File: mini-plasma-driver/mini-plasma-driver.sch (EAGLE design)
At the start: 36 parts, among them IC1 IR21844D, IC2 74LS19N, IC3 NE555N, Q1 IRF640, Q2 IRF640, Q3 2N2369, Q4 2N2369

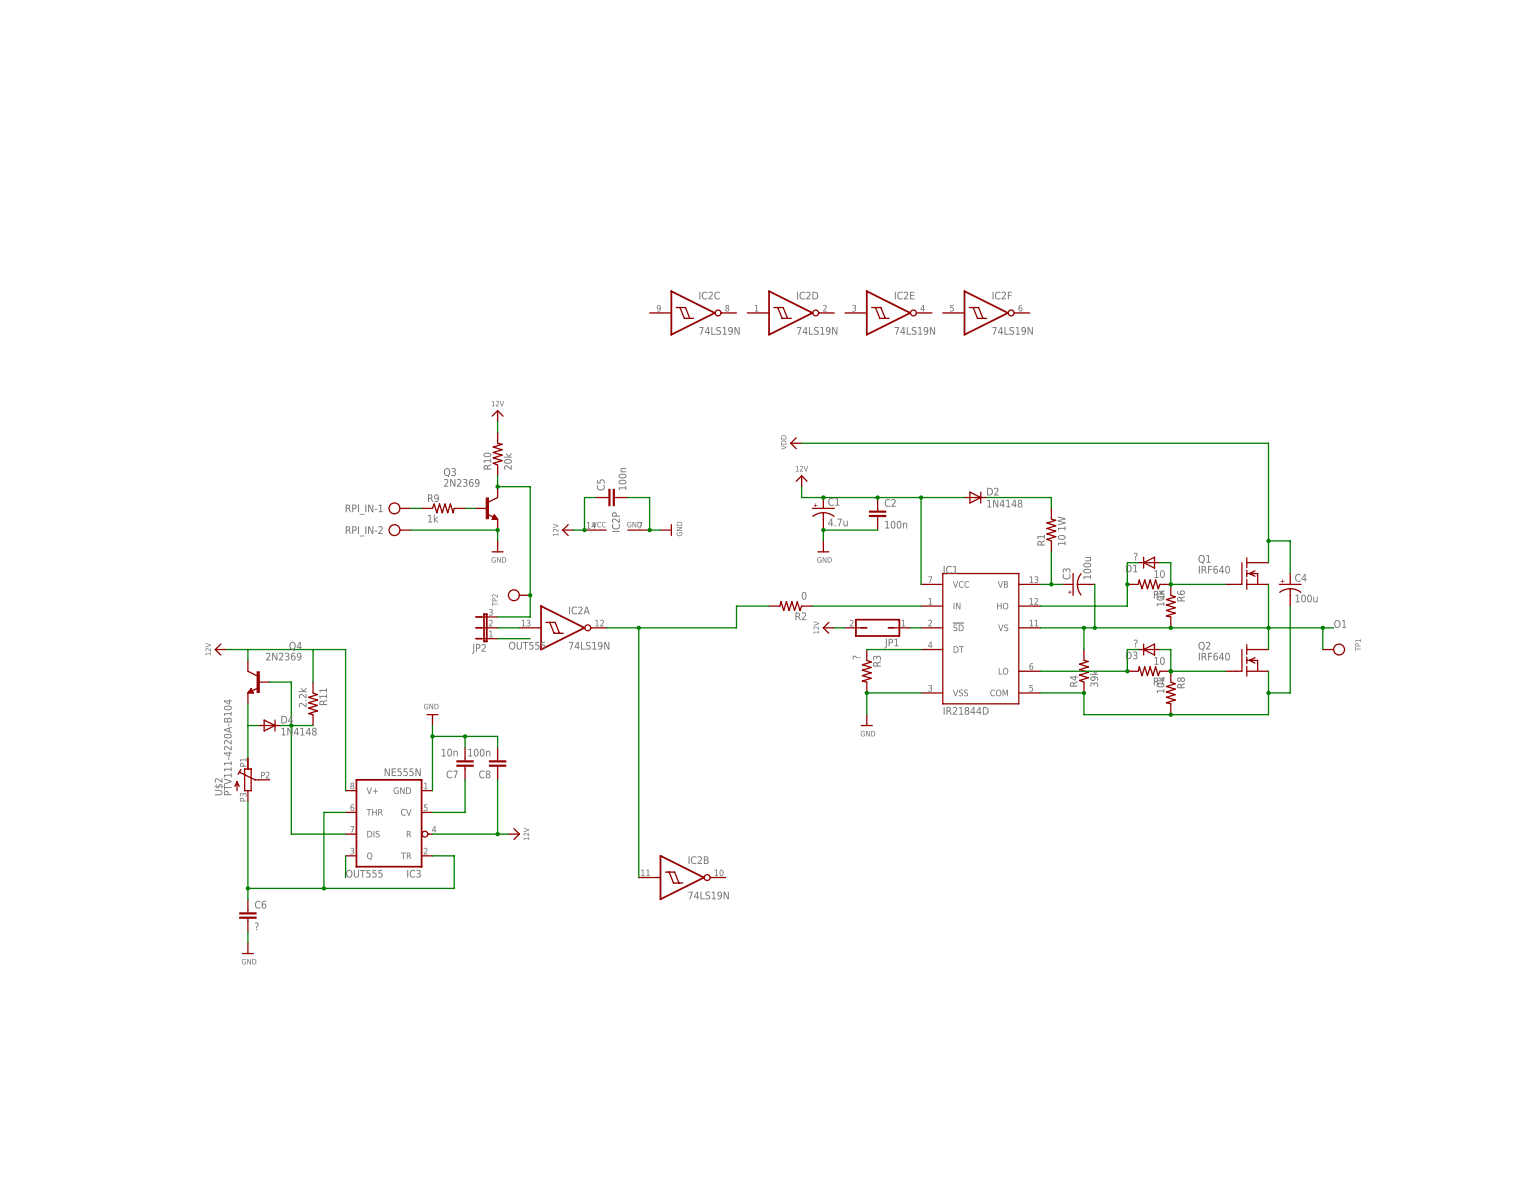
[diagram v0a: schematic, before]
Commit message: mini-plasma-driver
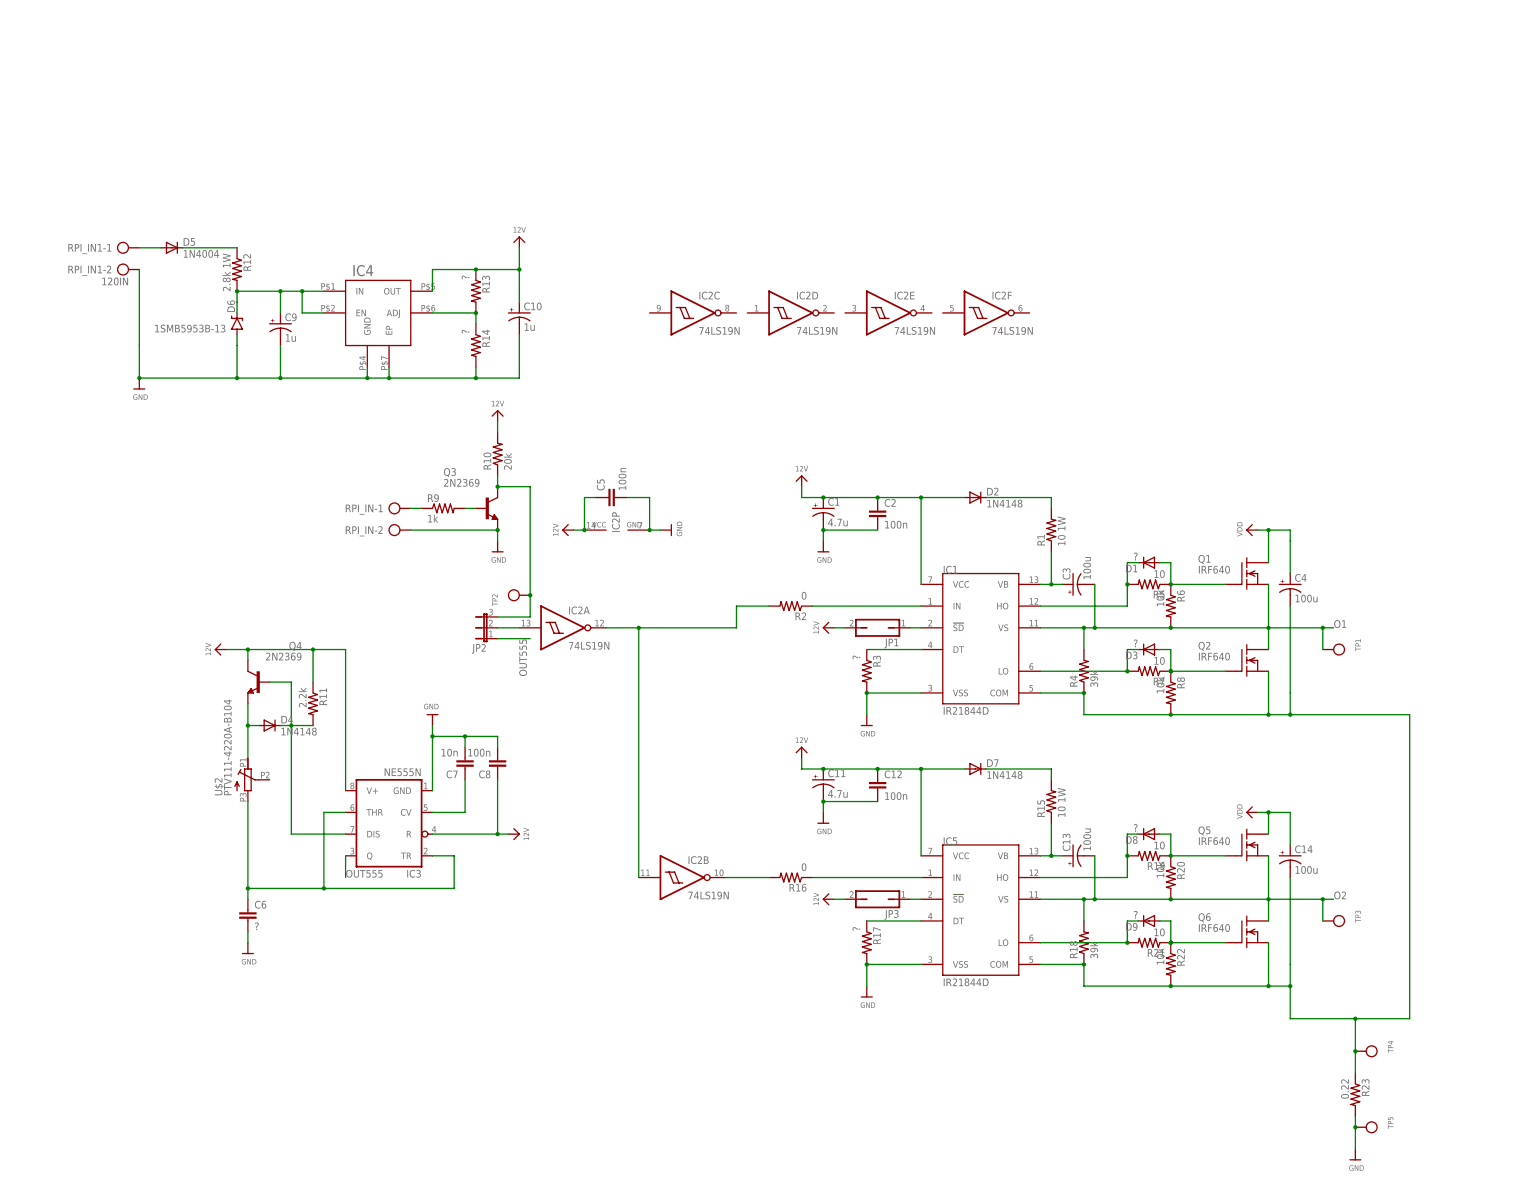
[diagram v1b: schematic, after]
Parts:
- added C10, C9: 1u, rcl:CPOL-USE2.5-5
- added C11: 4.7u, rcl:CPOL-USE2.5-5
- added C12: 100n, rcl:C-EU025-025X050
- added C13, C14: 100u, rcl:CPOL-USE3.5-10
- added D5: 1N4004, adafruit:1N4004
- added D6: 1SMB5953B-13, SparkFun-DiscreteSemi:DIODE-ZENERSMB
- added D7: 1N4148, diode:1N4148DO35-10
- added D8, D9: ?, diode:1N4148DO35-10
- added IC4: NCP781IC, keves-ng:NCP781IC
- added IC5: IR21844D, irs:IR21844D
- added JP3: (no value), jumper:JP1Q
- added Q5, Q6: IRF640, transistor-fet:IRF620
- added R12: 2.8k 1W, rcl:R-US_0207/10
- added R13, R14, R17: ?, rcl:R-US_0207/10
- added R15: 10 1W, rcl:R-US_0207/10
- added R16: 0, rcl:R-US_0207/10
- added R18: 39k, rcl:R-US_0207/10
- added R19, R21: 10, rcl:R-US_0207/10
- added R20, R22: 10k, rcl:R-US_0207/10
- added R23: 0.22, rcl:R-US_0207/10
- added RPI_IN1: 120IN, con-ptr500:AK500/2
- added TP3, TP4, TP5: (no value), microbuilder:TESTPOINT0.1"
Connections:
- new net N$18: D5.A, RPI_IN1-1.KL
- new net N$19: D5.C, R12.1
- new net N$20: C9.+, D6.C, IC4.EN, IC4.IN, R12.2
- new net N$21: D7.C, R15.2
- new net N$22: IC4.ADJ, R13.2, R14.1
- new net N$23: IC5.IN, R16.1
- new net N$24: IC2B.O, R16.2
- new net N$25: IC5.!SD, JP3.1
- new net N$26: IC5.DT, R17.1
- new net N$27: D8.C, IC5.HO, R19.2
- new net N$28: D8.A, Q5.G, R19.1, R20.1
- new net N$29: D9.C, IC5.LO, R21.2
- new net N$30: D9.A, Q6.G, R21.1, R22.1
- new net O2: C13.-, IC5.VS, Q5.S, Q6.D, R18.2, R20.2, TP3.P$1
- net 12V: now also C10.+, C11.+, C12.1, D7.A, IC4.OUT, IC5.VCC, JP3.2, R13.1
- net COM: now also C14.-, IC5.COM, Q6.S, R18.1, R22.2, R23.1, TP4.P$1
- net GND: now also C10.-, C11.-, C12.2, C9.-, D6.A, IC4.EP, IC4.GND, IC5.VSS, R14.2, R17.2, R23.2, RPI_IN1-2.KL, TP5.P$1
- net VB: now also C13.+, IC5.VB, R15.1
- net VDD: now also C14.+, Q5.D

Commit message: fixes after jeff's review
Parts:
- removed JP1, JP3: (no value), jumper:JP1Q
- added C15, C16: 1u Low ESR, rcl:C-EU025-025X050
- added C17, C18: 100n, rcl:C-EU025-025X050
- added R24, R25: 10 1W, rcl:R-US_0207/10
- added TP6: (no value), microbuilder:TESTPOINT0.1"
- C13, C3: value 100u -> 100n; device rcl:CPOL-USE3.5-10 -> rcl:C-EU025-025X050
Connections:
- removed net N$25: IC5.!SD, JP3.1
- new net SD: IC1.!SD, IC5.!SD, TP6.P$1
- net 12V: now also C15.2, C16.2; no longer JP1.2, JP3.2
- net COM: now also C15.1, C16.1, R24.2, R25.2; no longer C14.-, C4.-, Q2.S, Q6.S, R22.2, R23.1, R8.2, TP4.P$1
- net N$2: now also C14.-, C4.-, Q2.S, Q6.S, R22.2, R23.1, R24.1, R25.1, R8.2, TP4.P$1; no longer IC1.!SD, JP1.1
- net O1: now also C17.2, C3.2; no longer C3.-
- net O2: now also C13.2, C18.2; no longer C13.-
- net VB: now also C13.1, C17.1, C18.1, C3.1; no longer C13.+, C3.+
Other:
- moved on the sheet: R1, R15
